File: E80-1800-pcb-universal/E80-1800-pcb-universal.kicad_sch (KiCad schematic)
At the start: 48 parts, among them J1 SPI, J2 BATT, J3 OLED, J4 USB_C_Receptacle_USB2.0, Q1 Q_NMOS_GSD, SW1 RST, SW2 BOOT, U1 SRV05-4, U2 XC6206P332MR, U3 STM32F072RBTx

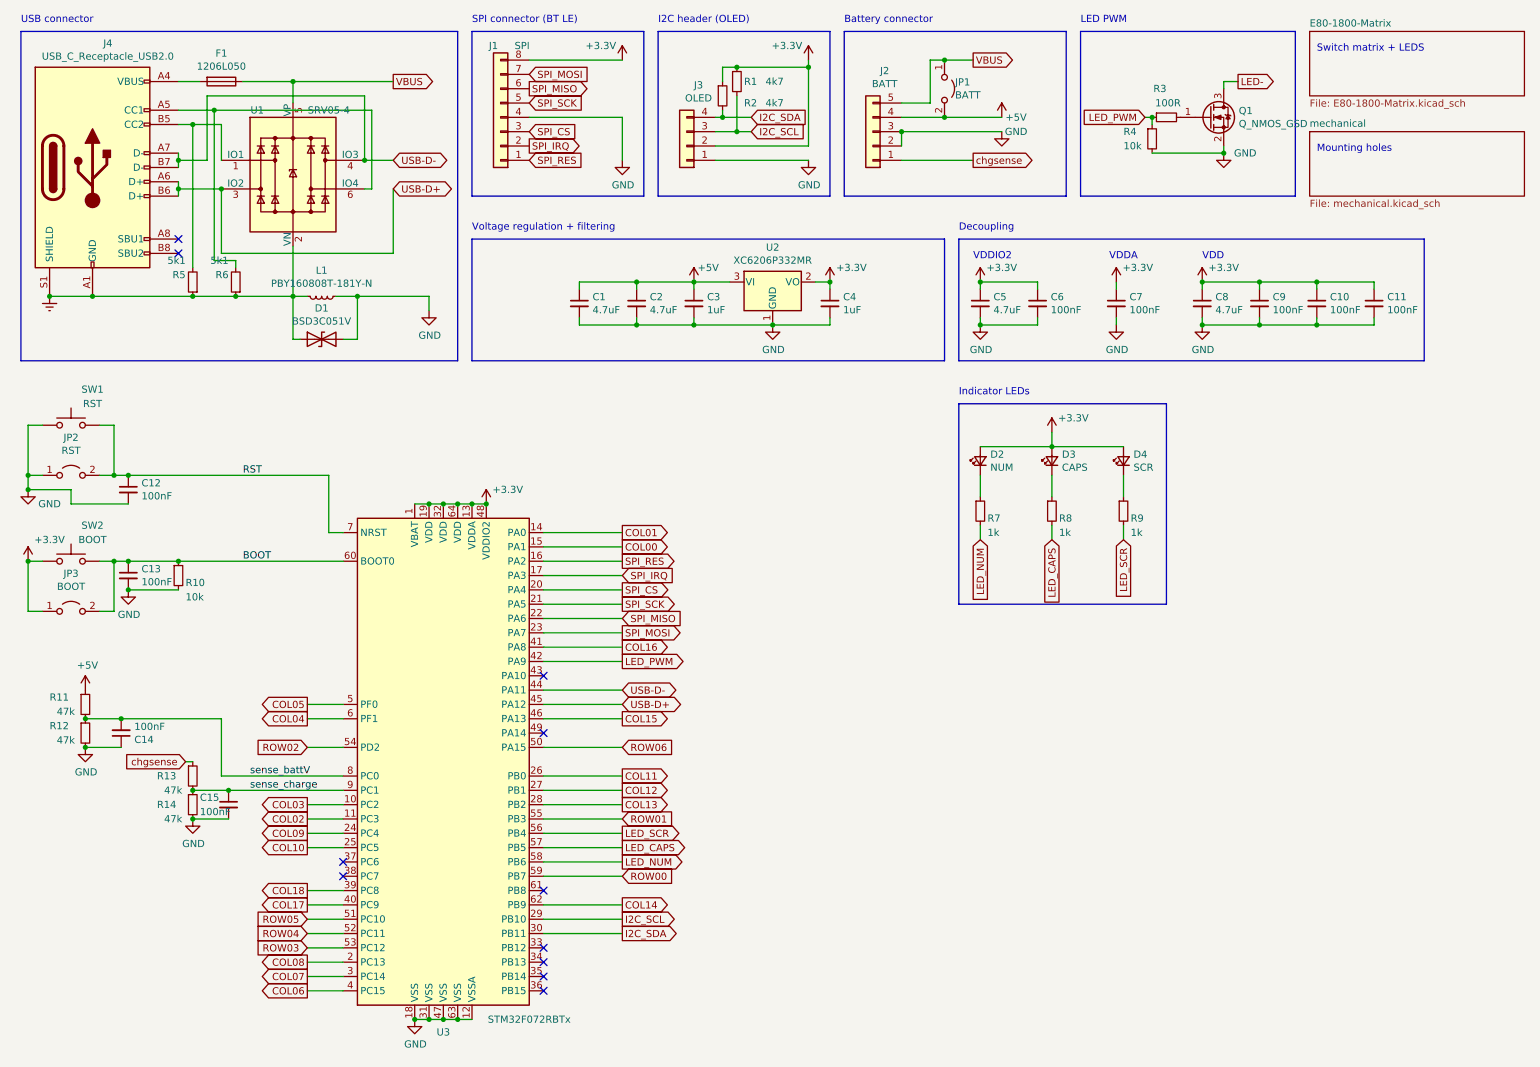
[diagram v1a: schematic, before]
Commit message: update to PCM marbastlib and KC8
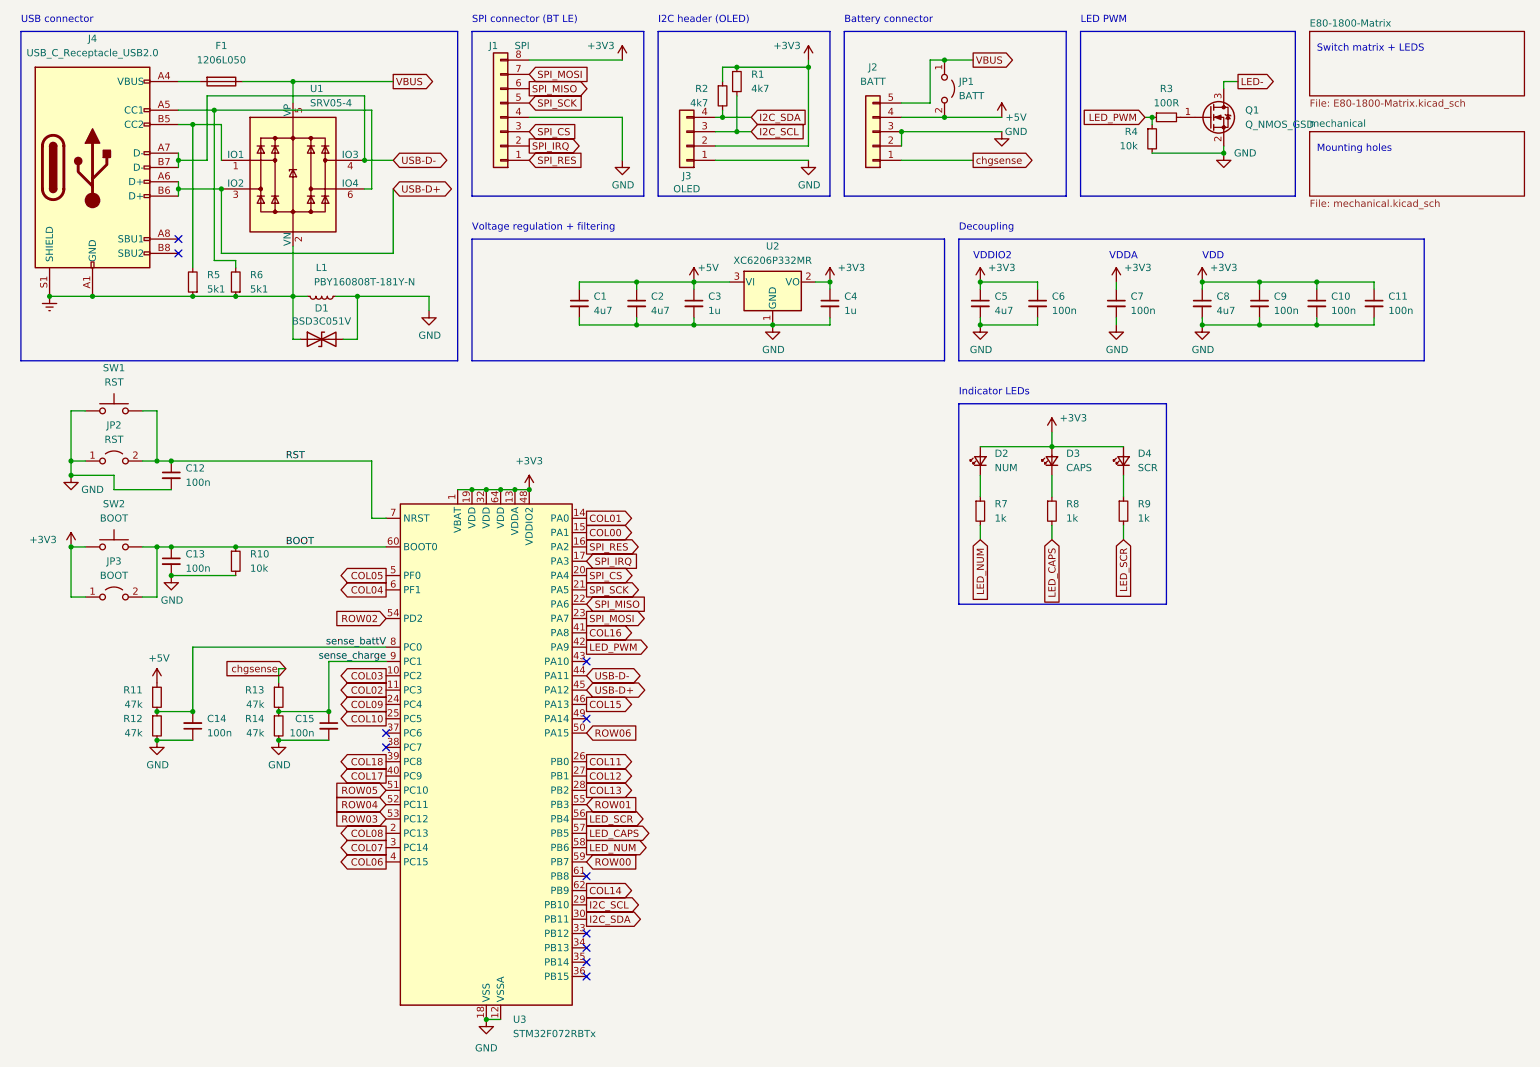
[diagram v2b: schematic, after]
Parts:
- C1, C2, C5, C8: value 4.7uF -> 4u7
- C10, C11, C12, C13, C14, C15, C6, C7, C9: value 100nF -> 100n
- C3, C4: value 1uF -> 1u
- J4: footprint Connector_USB:USB_C_Receptacle_HRO_TYPE-C-31-M-12 -> PCM_marbastlib-various:USB_C_Receptacle_HRO_TYPE-C-31-M-12
- SW1, SW2: footprint Button_Switch_SMD:SW_SPST_SKQG_WithoutStem -> PCM_marbastlib-various:SW_SPST_SKQG_WithStem
- U1: footprint Package_TO_SOT_SMD:SOT-23-6 -> PCM_marbastlib-various:SOT-23-6-routable
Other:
- moved on the sheet: C12, C13, C14, C15, JP2, JP3, R10, R11, R12, R13, R14, SW1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
